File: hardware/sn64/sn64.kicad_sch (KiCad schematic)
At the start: 2 parts, among them J1 N64_Cartridge_Edge_50, J2 SNES_Female_Slot_62

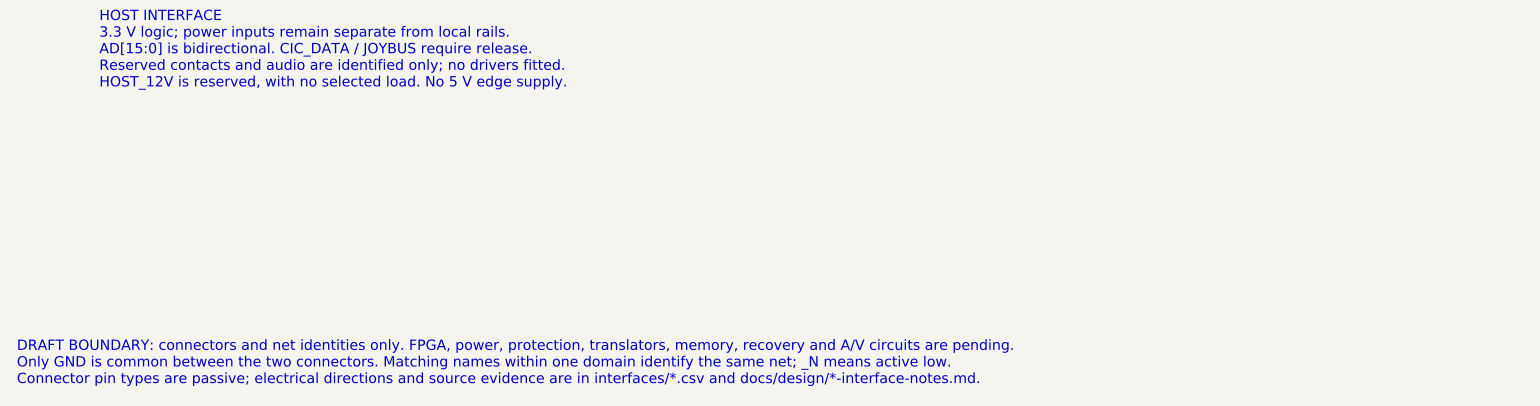
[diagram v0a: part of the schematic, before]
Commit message: Add side USB-C programming circuit and document source-checked interfaces
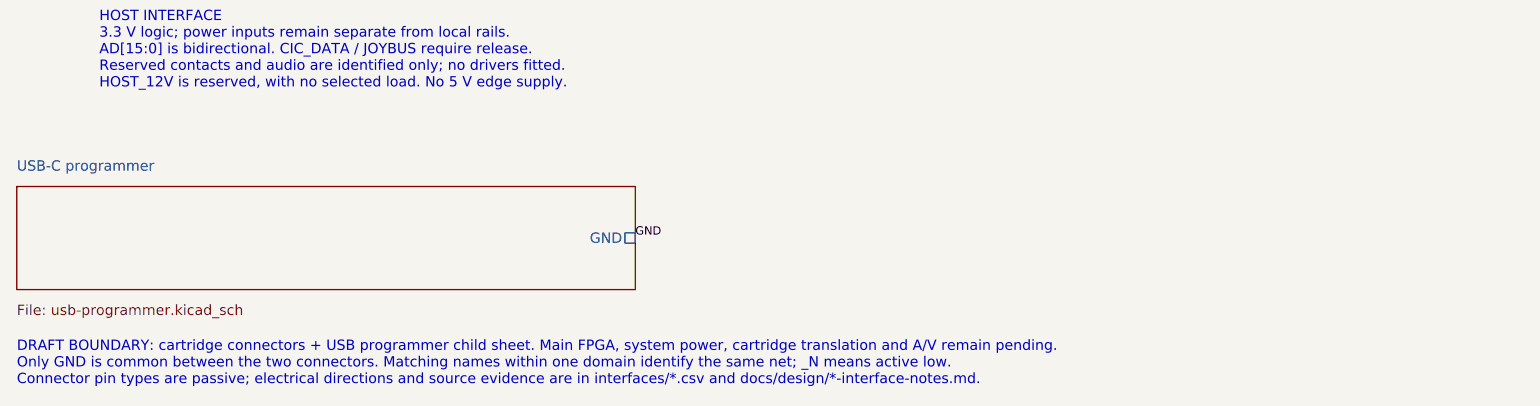
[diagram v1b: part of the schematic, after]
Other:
- added sheet USB-C programmer (usb-programmer.kicad_sch)
- note added: "DRAFT BOUNDARY: cartridge connectors + USB programmer child sheet. Main FPGA, system power, cartridge translation and A/V remain pending. Only GND is common between the two connectors. Matching names within one domain identify the same net; _N means active low. Connector pin types are passive; electrical directions and source evidence are in interfaces/*.csv and docs/design/*-interface-notes.md."
- note removed: "DRAFT BOUNDARY: connectors and net identities only. FPGA, power, protection, translators, memory, recovery and A/V circuits are pending. Only GND is common between the two connectors. Matching names within one domain identify the same net; _N means active low. Connector pin types are passive; electrical directions and source evidence are in interfaces/*.csv and docs/design/*-interface-notes.md."
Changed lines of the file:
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@@
-(kicad_sch (version 20250114) (generator "sn64_interface_builder") (paper "A3") (title_block (title "SN 64 - cartridge interfaces") (date "2026-09-28") (rev "0.1-interface") (company "SN 64") (comment 1 "INTERFACE DRAFT ONLY - NOT FOR MANUFACTURE") (comment 2 "Source attribution and limits: hardware/sn64/README.md"))
+(kicad_sch (version 20250114) (generator "sn64_interface_builder") (paper "A3") (title_block (title "SN 64 - cartridge interfaces") (date "2026-09-28") (rev "0.2-usb") (company "SN 64") (comment 1 "INTERFACE DRAFT ONLY - NOT FOR MANUFACTURE") (comment 2 "Source attribution and limits: hardware/sn64/README.md"))
 (symbol (lib_id "SN64:N64_Cartridge_Edge_50") (at 101.6 127 0) (unit 1) (exclude_from_sim no) (in_bom yes) (on_board yes) (dnp no)
 (property "Reference" "J1" (at 101.6 58.42 0) (effects (font (size 1.27 1.27))))
@@
 (text "HOST INTERFACE\n3.3 V logic; power inputs remain separate from local rails.\nAD[15:0] is bidirectional. CIC_DATA / JOYBUS require release.\nReserved contacts and audio are identified only; no drivers fitted.\nHOST_12V is reserved, with no selected load. No 5 V edge supply." (at 30.48 208.28 0) (effects (font (size 1.27 1.27)) (justify left top)))
 (text "SNES INTERFACE\n5 V cartridge logic requires reviewed translation and isolation.\nSNES_5V_CART: protected switched supply, default OFF (pending).\nSystem RESET must support cartridge assertion and input sensing.\nCIC_SLAVE_RESET is separate; AUDIO_L/R_IN are analog inputs.\nNo universal NC contacts. Full pin behavior is recorded in the CSV." (at 220.98 213.36 0) (effects (font (size 1.27 1.27)) (justify left top)))
-(text "DRAFT BOUNDARY: connectors and net identities only. FPGA, power, protection, translators, memory, recovery and A/V circuits are pending.\nOnly GND is common between the two connectors. Matching names within one domain identify the same net; _N means active low.\nConnector pin types are passive; electrical directions and source evidence are in interfaces/*.csv and docs/design/*-interface-notes.md." (at 20.32 248.92 0) (effects (font (size 1.27 1.27)) (justify left top)))
-(sheet_instances (path "/" (page "1"))) (embedded_fonts no))
+(text "DRAFT BOUNDARY: cartridge connectors + USB programmer child sheet. Main FPGA, system power, cartridge translation and A/V remain pending.\nOnly GND is common between the two connectors. Matching names within one domain identify the same net; _N means active low.\nConnector pin types are passive; electrical directions and source evidence are in interfaces/*.csv and docs/design/*-interface-notes.md." (at 20.32 248.92 0) (effects (font (size 1.27 1.27)) (justify left top)))
+(sheet_instances (path "/" (page "1"))) (embedded_fonts no)
+(sheet (at 20.32 229.87) (size 76.2 12.7) (stroke (width 0.1524) (type solid)) (fill (color 0 0 0 0)) (property "Sheetname" "USB-C programmer" (at 20.32 227.33 0) (effects (font (size 1.27 1.27)) (justify left)))(property "Sheetfile" "usb-programmer.kicad_sch" (at 20.32 245.11 0) (effects (font (size 1.27 1.27)) (justify left))) (pin "GND" passive (at 96.52 236.22 0) (effects (font (size 1.27 1.27)) (justify right))) (instances (project "sn64" (path "/e2505a21-9627-547b-aef4-ab0d2c57bd10" (page "2")))))
+(label "GND" (at 96.52 236.22 0) (effects (font (size 1.016 1.016)) (justify left bottom)))
+)
